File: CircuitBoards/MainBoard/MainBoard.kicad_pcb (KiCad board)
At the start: 2 copper layers, 203.2 x 170.2 mm, 16 parts, among them J1 39-28-1103, J29 ATA, J8 178-009-613, J901 DualMiniDin6

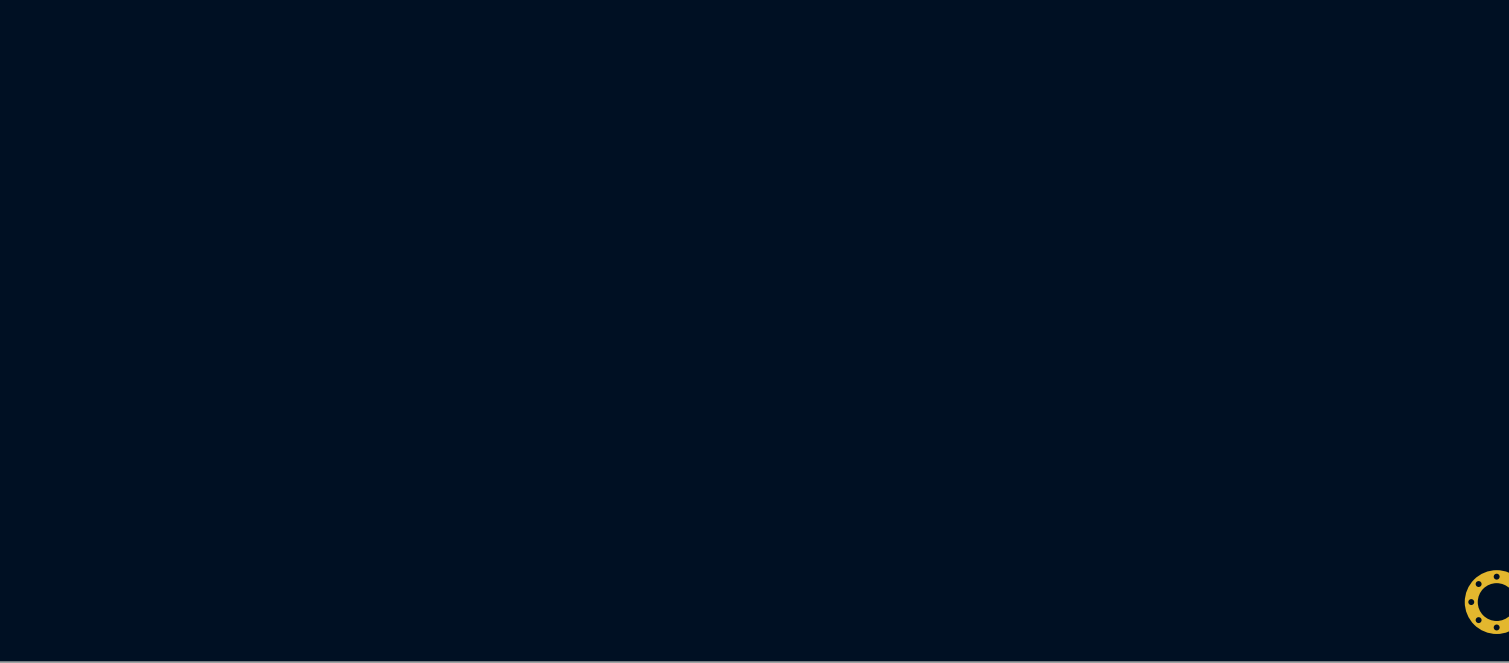
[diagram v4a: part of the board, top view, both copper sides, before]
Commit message: MainBoard: Addition of the DRAM schematics
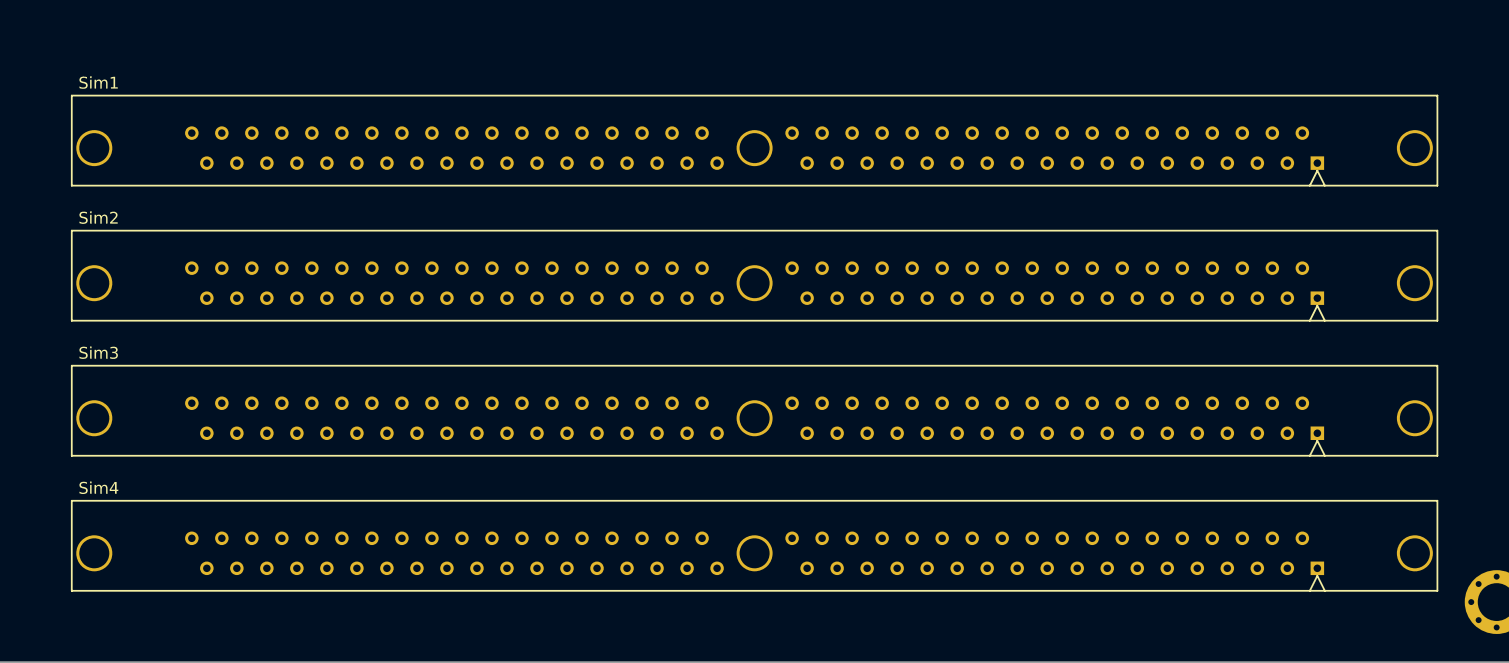
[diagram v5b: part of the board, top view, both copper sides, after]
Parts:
- added Sim1: Simm72, My68k:5822021-4, F.Cu at (180.9, 141.6)
- added Sim2: Simm72, My68k:5822021-4, F.Cu at (180.9, 153.0)
- added Sim3: Simm72, My68k:5822021-4, F.Cu at (180.9, 164.5)
- added Sim4: Simm72, My68k:5822021-4, F.Cu at (180.9, 175.9)

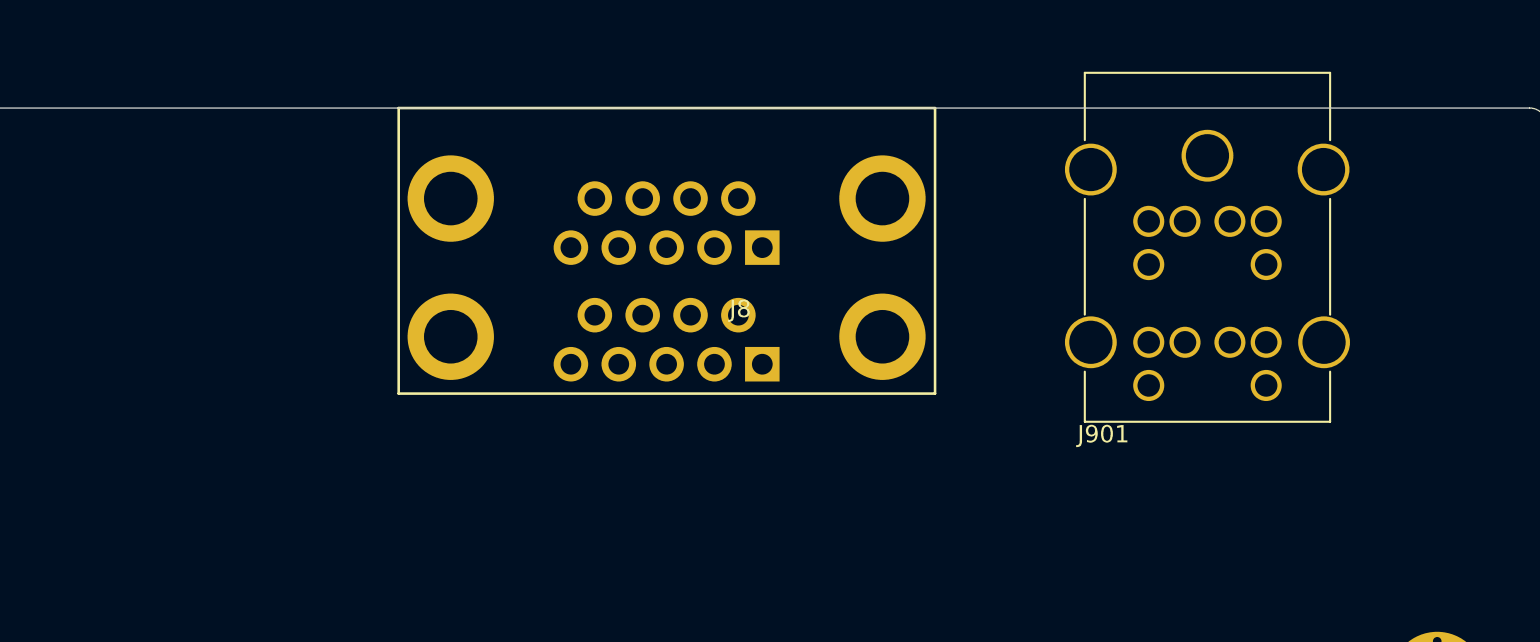
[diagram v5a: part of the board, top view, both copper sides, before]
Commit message: MainBoard: Addition of the Network schematic
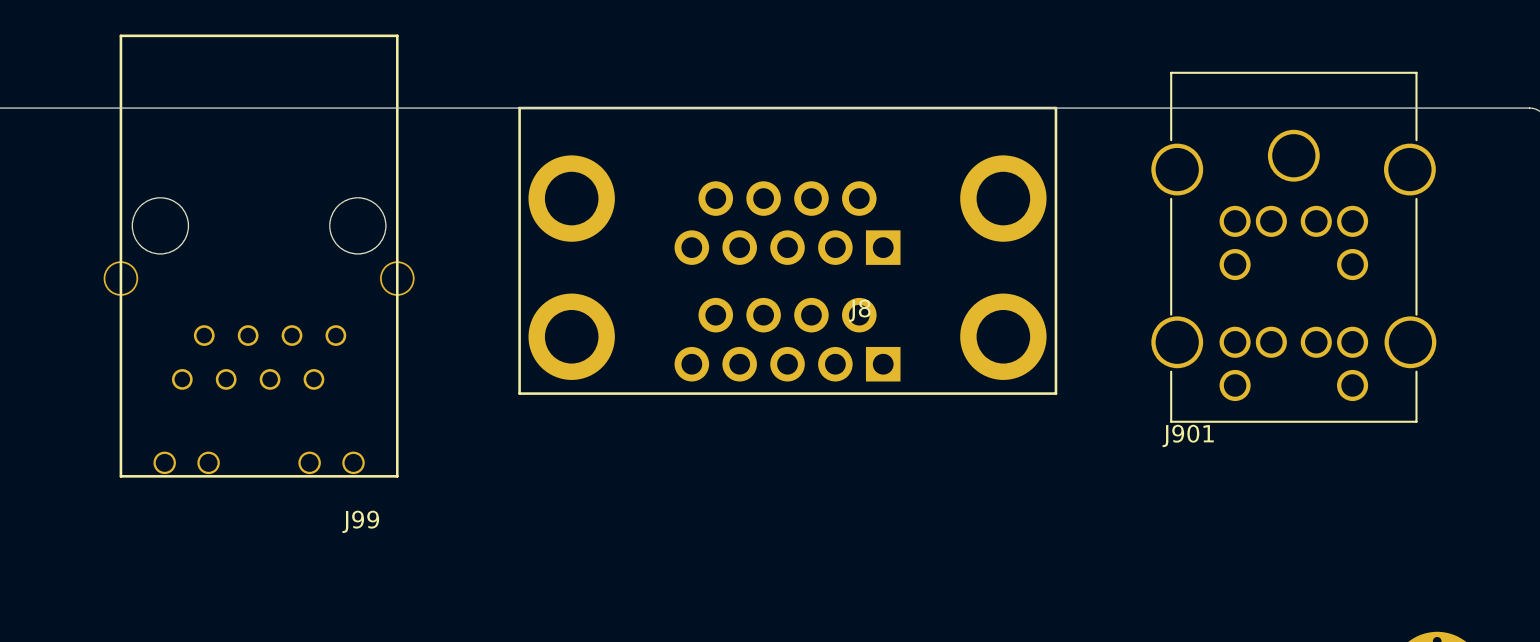
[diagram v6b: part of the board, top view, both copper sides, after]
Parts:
- added J99: 5-2301994-2, My68k:5-2301994-2, F.Cu at (175.6, 21.7)
- moved J8 7.00 mm to (211.7, 23.0)
- moved J901 5.00 mm to (235.4, 24.0)
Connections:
- J1 pad 10: (no net) -> +5Vsb
- J1 pad 5: (no net) -> nPS_On
